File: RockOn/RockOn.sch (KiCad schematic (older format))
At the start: 9 parts

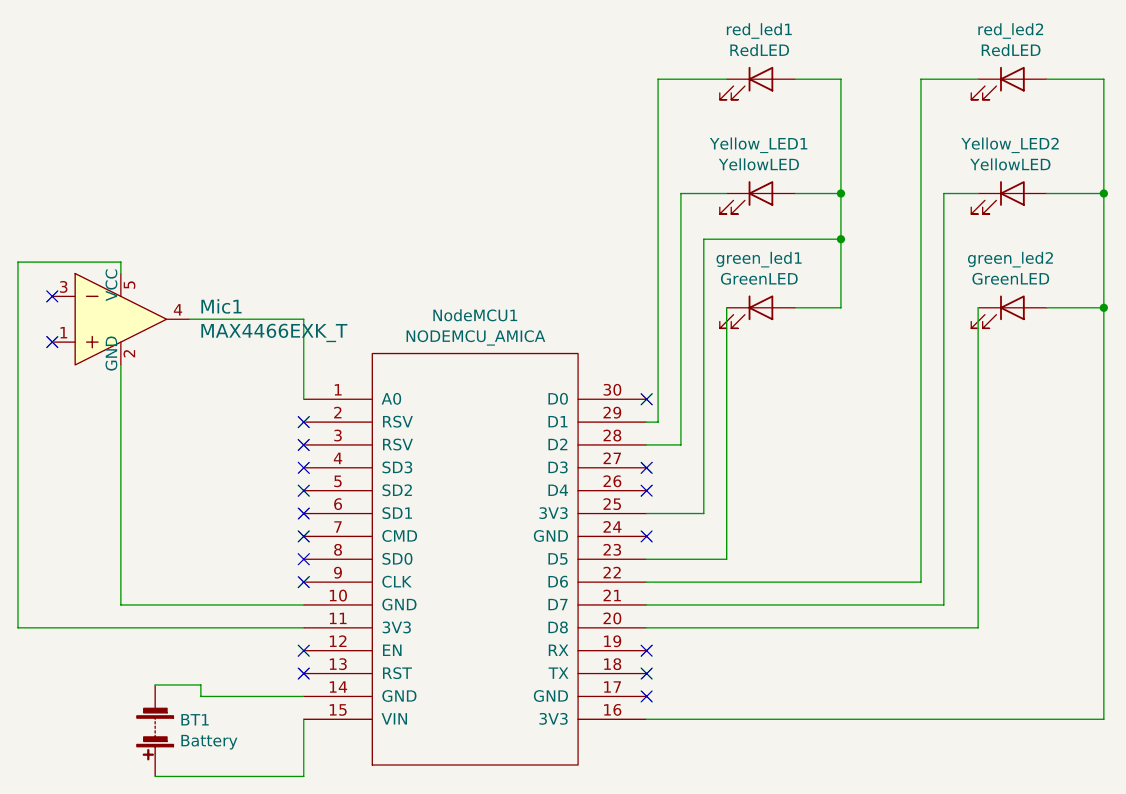
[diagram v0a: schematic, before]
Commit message: Corrected components, silkscreen
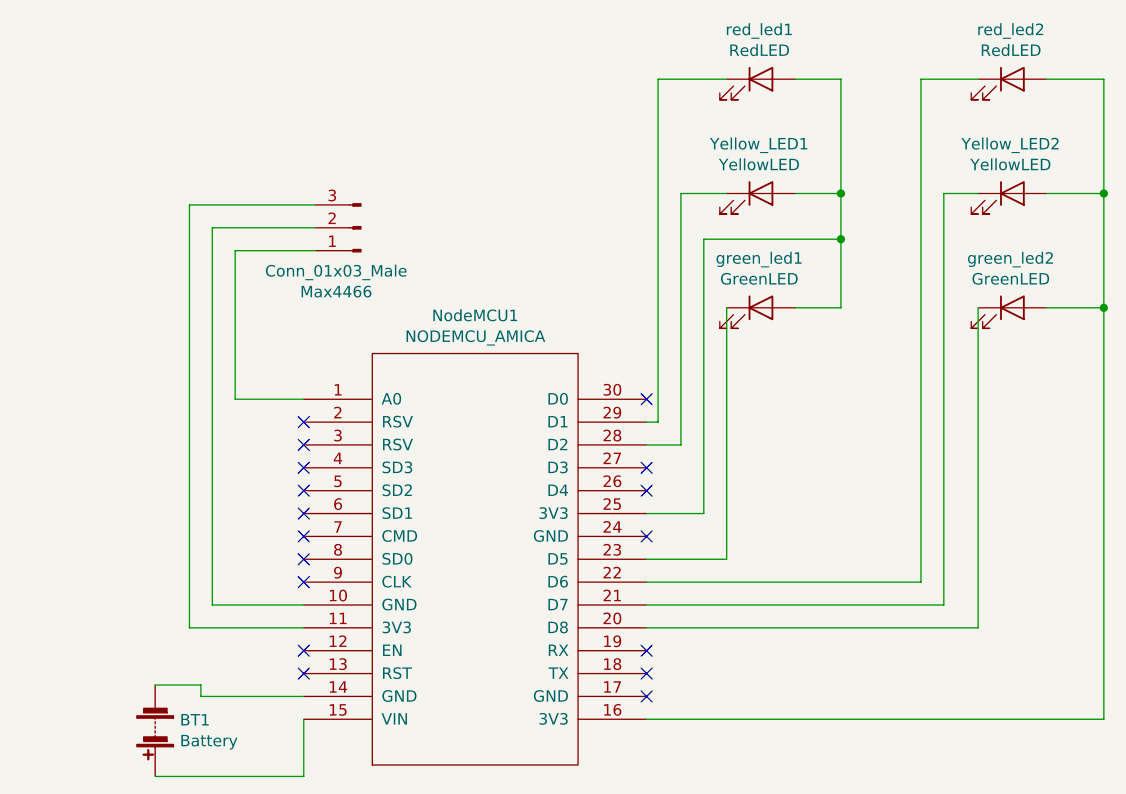
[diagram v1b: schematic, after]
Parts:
- removed Mic1: MAX4466EXK_T, digikey-footprints:SOT-353, symbol dk_Linear-Amplifiers-Audio:MAX4466EXK_T
- added Max4466: Conn_01x03_Male, symbol Connector:Conn_01x03_Male
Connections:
- net at NodeMCU1.1 (A0): now also Max4466.1 (Pin_1)
- net at NodeMCU1.10 (GND): now also Max4466.2 (Pin_2)
- net at NodeMCU1.11 (3V3): now also Max4466.3 (Pin_3)
- no-connect marks 19 -> 17
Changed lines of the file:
@@
-$EndComp
-$Comp
-L dk_Linear-Amplifiers-Audio:MAX4466EXK_T Mic1
-U 1 1 5E362ACD
-P 2300 3350
-F 0 "Mic1" H 2644 3403 60  0000 L CNN
-F 1 "MAX4466EXK_T" H 2644 3297 60  0000 L CNN
-F 2 "digikey-footprints:SOT-353" H 2500 3550 60  0001 L CNN
-F 3 "https://datasheets.maximintegrated.com/en/ds/MAX4465-MAX4469.pdf" H 2500 3650 60  0001 L CNN
-F 4 "MAX4466EXK+CT-ND" H 2500 3750 60  0001 L CNN "Digi-Key_PN"
-F 5 "MAX4466EXK+T" H 2500 3850 60  0001 L CNN "MPN"
-F 6 "Integrated Circuits (ICs)" H 2500 3950 60  0001 L CNN "Category"
-F 7 "Linear - Amplifiers - Audio" H 2500 4050 60  0001 L CNN "Family"
-F 8 "https://datasheets.maximintegrated.com/en/ds/MAX4465-MAX4469.pdf" H 2500 4150 60  0001 L CNN "DK_Datasheet_Link"
-F 9 "/product-detail/en/maxim-integrated/MAX4466EXK-T/MAX4466EXK-CT-ND/5405773" H 2500 4250 60  0001 L CNN "DK_Detail_Page"
-F 10 "IC PREAMP AUDIO MONO AB SC70-5" H 2500 4350 60  0001 L CNN "Description"
-F 11 "Maxim Integrated" H 2500 4450 60  0001 L CNN "Manufacturer"
-F 12 "Active" H 2500 4550 60  0001 L CNN "Status"
-	1    2300 3350
-	1    0    0    -1
 $EndComp
 $Comp
@@
 	1    0    0    -1
 $EndComp
-Wire Wire Line
-	2600 3350 3100 3350
-Wire Wire Line
-	3100 3350 3100 3700
 $Comp
 L Device:LED red_led1
@@
 NoConn ~ 4600 4000
 NoConn ~ 4600 3700
-Wire Wire Line
-	3100 4600 2300 4600
-Wire Wire Line
-	2300 4600 2300 3550
-Wire Wire Line
-	3100 4700 1850 4700
-Wire Wire Line
-	1850 4700 1850 3100
-Wire Wire Line
-	1850 3100 2300 3100
-Wire Wire Line
-	2300 3100 2300 3150
-NoConn ~ 2000 3250
-NoConn ~ 2000 3450
+$Comp
+L Connector:Conn_01x03_Male Max4466
+U 1 1 5E383425
+P 3350 2950
+F 0 "Max4466" H 3458 3231 50  0000 C CNN
+F 1 "Conn_01x03_Male" H 3458 3140 50  0000 C CNN
+F 2 "" H 3350 2950 50  0001 C CNN
+F 3 "~" H 3350 2950 50  0001 C CNN
+	1    3350 2950
+	-1   0    0    1
+$EndComp
+Wire Wire Line
+	3100 3700 2800 3700
+Wire Wire Line
+	2800 3700 2800 3050
+Wire Wire Line
+	2800 3050 3150 3050
+Wire Wire Line
+	3100 4600 2700 4600
+Wire Wire Line
+	2700 4600 2700 2950
+Wire Wire Line
+	2700 2950 3150 2950
+Wire Wire Line
+	3100 4700 2600 4700
+Wire Wire Line
+	2600 4700 2600 2850
+Wire Wire Line
+	2600 2850 3150 2850
 $EndSCHEMATC

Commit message: larger silkscreen
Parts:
- BT1: footprint Battery_Holders:Bulgin_BX0036_1xC -> Battery_Holders:Keystone_2479_3xAAA
- Max4466: footprint (none) -> Connectors:PINHEAD1-3
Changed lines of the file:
@@
 F 0 "BT1" H 2342 5104 50  0000 R CNN
 F 1 "Battery" H 2342 5195 50  0000 R CNN
-F 2 "Battery_Holders:Bulgin_BX0036_1xC" V 2450 5210 50  0001 C CNN
+F 2 "Battery_Holders:Keystone_2479_3xAAA" V 2450 5210 50  0001 C CNN
 F 3 "~" V 2450 5210 50  0001 C CNN
 	1    2450 5150
@@
 F 0 "Max4466" H 3458 3231 50  0000 C CNN
 F 1 "Conn_01x03_Male" H 3458 3140 50  0000 C CNN
-F 2 "" H 3350 2950 50  0001 C CNN
+F 2 "Connectors:PINHEAD1-3" H 3350 2950 50  0001 C CNN
 F 3 "~" H 3350 2950 50  0001 C CNN
 	1    3350 2950

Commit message: Partially routed
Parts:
- NodeMCU1: footprint ESP8266:NodeMCU1.0(12-E) -> ESP8266:NodeMCU-LoLinV3
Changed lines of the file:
@@
 F 0 "NodeMCU1" H 3850 5465 50  0000 C CNN
 F 1 "NODEMCU_AMICA" H 3850 5374 50  0000 C CNN
-F 2 "ESP8266:NodeMCU1.0(12-E)" H 3850 3350 50  0001 C CNN
+F 2 "ESP8266:NodeMCU-LoLinV3" H 3850 3350 50  0001 C CNN
 F 3 "" H 3850 3250 50  0001 C CNN
 	1    3850 4400
